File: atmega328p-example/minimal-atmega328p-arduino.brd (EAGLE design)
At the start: 90 x 40 mm, 27 parts, among them J1 3x2 M, J2 1x6 M, J4 POWER_JACK, U1 NCP1117ST50T3G, U4 ATMEGA328P-PU, Y1 16 MHz

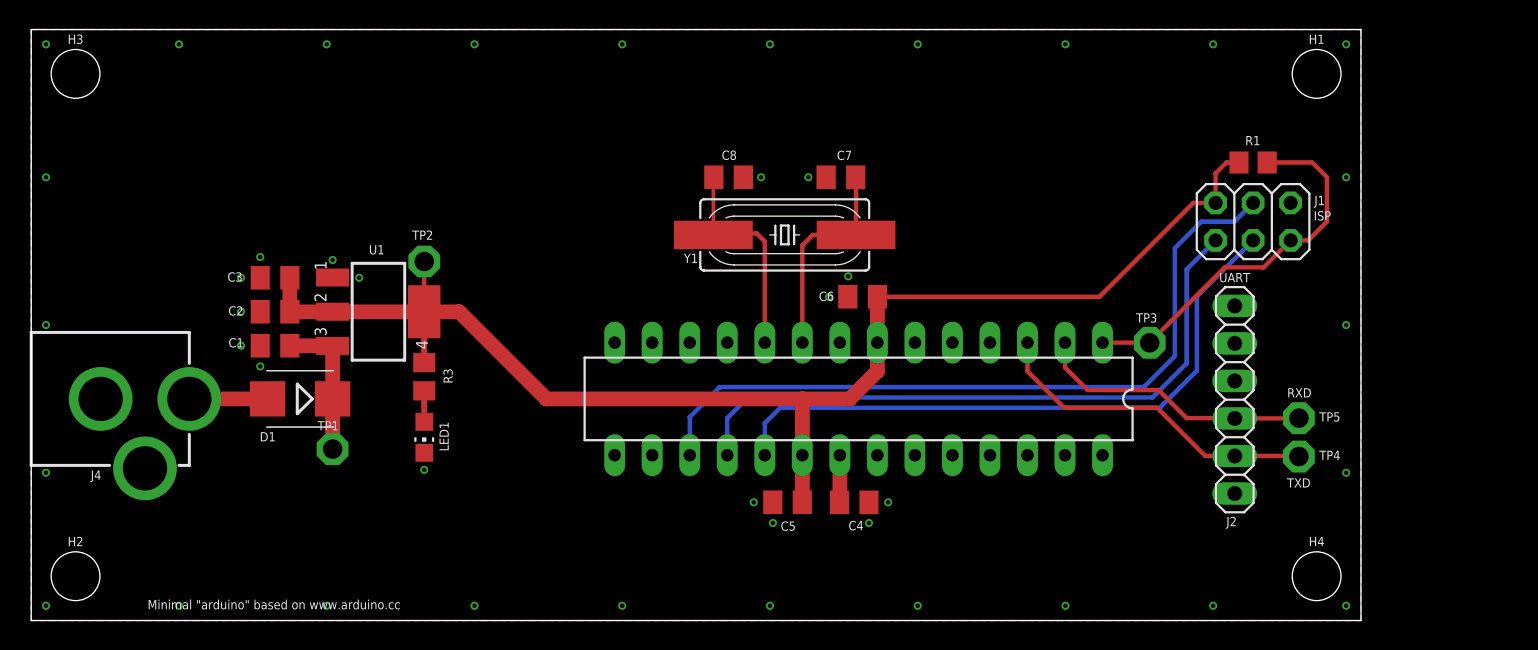
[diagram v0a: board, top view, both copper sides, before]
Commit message: Added microusb connector for power with DNP zero ohms, updated BOM.
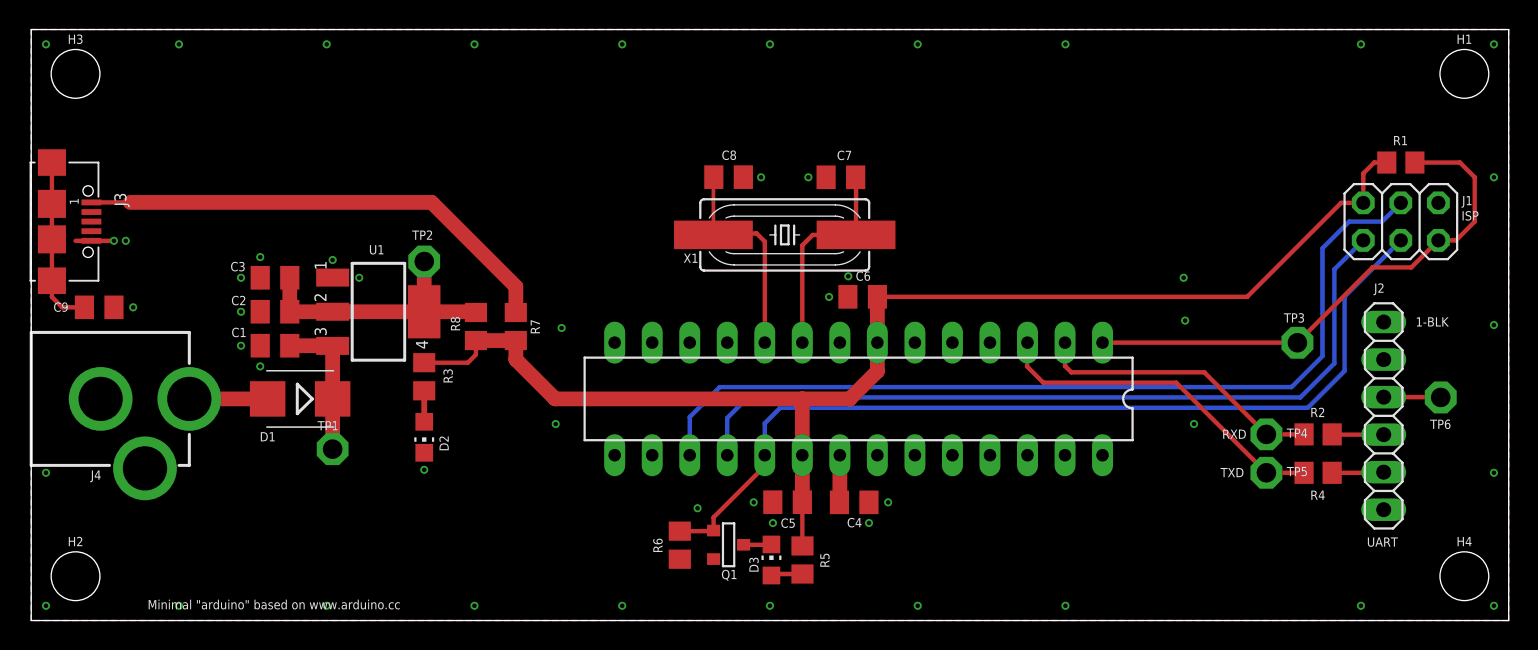
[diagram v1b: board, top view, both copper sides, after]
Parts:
- added C9: 100n, rcl:C0805K
- added D3: GREEN, led:CHIP-LED0805
- added J3: 629105136821, Wurth_Elektronik_Electromechanic_Input-Output_Connectors_rev19b:629105136821
- added Q1: PMV45EN2R, zetex:SOT-23
- added R2, R4, R5: 1K, rcl:R0805
- added R6: 10K, rcl:R0805
- added R7, R8: DNP or 0, rcl:R0805
- added TP6: TPPAD1-13, testpad:P1-13
- moved J2 10.1 mm to (91.5, 13.9), turned to 270 degrees
- moved H1 10.0 mm to (97.0, 37.0)
- moved H4 10.0 mm to (97.0, 3.00)
- moved J1 10.0 mm to (92.7, 27.0)
- moved R1 10.0 mm to (92.7, 31.0)
- moved TP3 10.0 mm to (85.7, 18.8)
- moved TP5 4.30 mm to (83.6, 10.0)
- moved TP4 2.66 mm to (83.6, 12.6)
- renumbered LED1 to D2, Y1 to X1
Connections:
- removed net RXD: J2.3, TP5.TP, U4.2
- removed net TXD: J2.2, TP4.TP, U4.3
- new net 5VEXT: C2.2, C3.1, R8.2, TP2.TP, U1.2, U1.4
- new net AVR-RXD: R2.2, TP4.TP, U4.2
- new net AVR-TXD: R4.2, TP5.TP, U4.3
- new net FTDI-RXD: J2.5, R4.1
- new net FTDI-TXD: J2.4, R2.1
- new net N$2: D3.A, R5.1
- new net N$4: D3.C, Q1.1
- new net N$5: J2.3, TP6.TP
- new net N$6: C9.2, J3.SHELL, J3.SHELL1, J3.SHELL2, J3.SHELL3
- new net VUSB: J3.1, R7.2
- net +5V: now also R5.2, R7.1, R8.1; no longer C2.2, C3.1, TP2.TP, U1.2, U1.4
- net GND: now also C9.1, J2.1, J3.5, Q1.2, R6.1; no longer J2.6
- net SCK: now also Q1.3, R6.2
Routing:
- net VUSB: track 0.00 -> 32.8 mm
- net AVR-TXD: track 0.00 -> 23.4 mm
- net TXD: track 22.7 -> 0.00 mm
- net AVR-RXD: track 0.00 -> 19.7 mm
- net RXD: track 18.9 -> 0.00 mm
- net SCK: track 43.3 -> 62.1 mm
- net 5VEXT: track 0.00 -> 18.3 mm
- net N$6: track 0.00 -> 11.6 mm
- net !RESET: track 26.1 -> 36.1 mm
- net MOSI: track 51.0 -> 61.0 mm
- net MISO: track 44.3 -> 54.3 mm
- net +5V: track 93.6 -> 89.4 mm
- net N$5: track 0.00 -> 3.87 mm
- net FTDI-RXD: track 0.00 -> 3.51 mm
- net FTDI-TXD: track 0.00 -> 3.50 mm
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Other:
- board size 90 x 40 mm -> 100 x 40 mm
- board text added: "1-BLK"

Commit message: Added reset switch, moved programming wires to bottom layer.
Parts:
- added SW1: !RESET, SparkFun-Electromechanical:TACTILE_SWITCH_SMD
- moved TP3 9.80 mm to (75.9, 18.8)
- moved J2 0.50 mm to (91.5, 13.4)
- moved R2 0.50 mm to (87.1, 12.1)
- moved R4 0.50 mm to (87.1, 9.50)
- moved TP4 0.50 mm to (83.6, 12.1)
- moved TP5 0.50 mm to (83.6, 9.50)
- moved TP6 0.50 mm to (95.4, 14.6)
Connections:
- net !RESET: now also SW1.3
- net GND: now also SW1.1
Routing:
- net +5V: track 89.4 -> 98.5 mm
- net !RESET: track 36.1 -> 39.6 mm
- net GND: vias 49 -> 50
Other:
- board text added: "ECE411 328 Board Rev 1 Based on Arduino UNO Rev 3 CC by-SA"
- board text removed: "Minimal "arduino" based on www.arduino.cc"
